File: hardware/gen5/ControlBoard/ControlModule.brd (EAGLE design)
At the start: 39 x 65.3 mm, 44 parts, among them Q1 BSS123, Q2 BSS123, U1 ATMEGA328P-AU

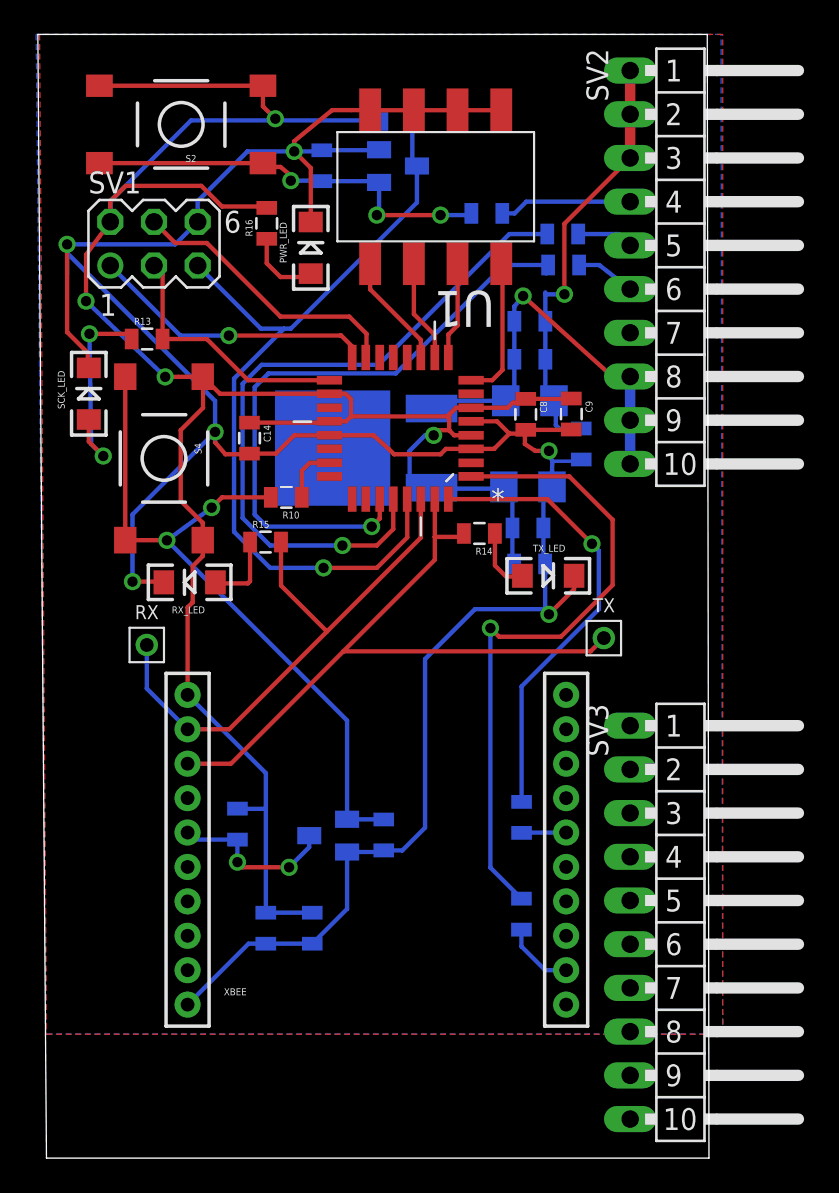
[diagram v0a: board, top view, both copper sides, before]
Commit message: connected plane to gnd and straightened out board outlines
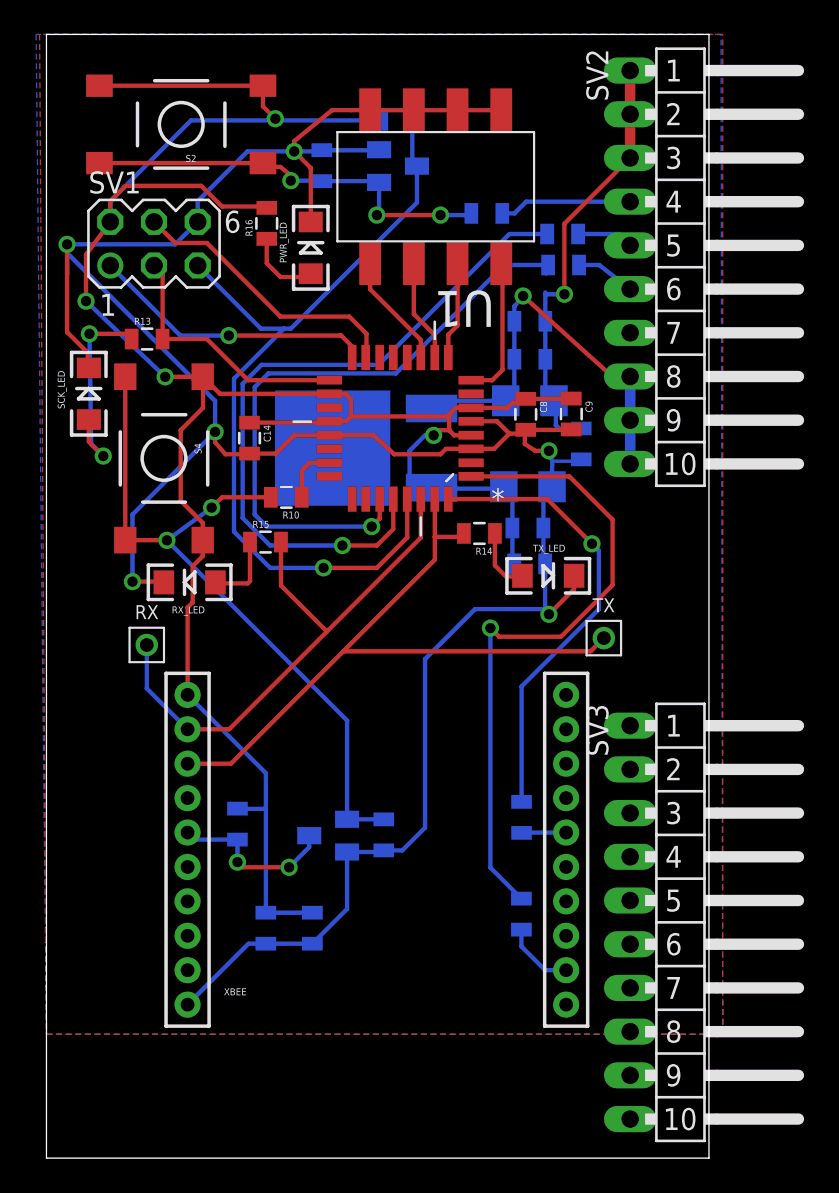
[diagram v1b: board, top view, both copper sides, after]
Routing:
- added copper zone on layer 1, net GND
- added copper zone on layer 16, net GND
- removed copper zone on layer 1, net N$4
- removed copper zone on layer 16, net N$6
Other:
- board size 39 x 65.3 mm -> 38.5 x 65.3 mm
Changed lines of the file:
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@@
 <?xml version="1.0" encoding="utf-8"?>
 <!DOCTYPE eagle SYSTEM "eagle.dtd">
-<eagle version="7.4.0">
+<eagle version="7.2.0">
 <drawing>
 <settings>
@@
 <plain>
 <wire x1="0" y1="0" x2="38.5" y2="0" width="0" layer="20"/>
-<wire x1="38.5" y1="0" x2="38.4" y2="65.3" width="0" layer="20"/>
-<wire x1="38.4" y1="65.3" x2="-0.5" y2="65.3" width="0" layer="20"/>
-<wire x1="-0.5" y1="65.3" x2="0" y2="0" width="0" layer="20"/>
+<wire x1="38.5" y1="0" x2="38.5" y2="65.3" width="0" layer="20"/>
+<wire x1="38.5" y1="65.3" x2="0" y2="65.3" width="0" layer="20"/>
+<wire x1="0" y1="65.3" x2="0" y2="0" width="0" layer="20"/>
 <dimension x1="38.5" y1="0" x2="38.4" y2="65.3" x3="51.11475" y3="32.66939375" textsize="1.778" layer="20" unit="inch"/>
 <dimension x1="39.2" y1="65.3" x2="-0.6" y2="65.3" x3="19.3" y3="70" textsize="1.778" layer="20" unit="inch"/>
@@
 <wire x1="29.4" y1="40.5" x2="30.98" y2="40.5" width="0.2032" layer="16"/>
 <wire x1="30.98" y1="40.5" x2="31.08" y2="40.6" width="0.2032" layer="16"/>
-<wire x1="16.4416" y1="42" x2="16.63" y2="41.26" width="0" layer="19" extent="1-16"/>
+<polygon width="0.254" layer="1">
+<vertex x="0" y="7.2"/>
+<vertex x="39.3" y="7.2"/>
+<vertex x="39.3" y="65.3"/>
+<vertex x="-0.4" y="65.3"/>
+</polygon>
+<polygon width="0.254" layer="16">
+<vertex x="0" y="7.2"/>
+<vertex x="39.3" y="7.2"/>
+<vertex x="39.2" y="65.3"/>
+<vertex x="-0.6" y="65.3"/>
+</polygon>
 </signal>
 <signal name="3.3V">
@@
 <wire x1="31.08" y1="42.4" x2="29.8" y2="42.4" width="0.2032" layer="16"/>
 </signal>
-<signal name="N$4">
-<polygon width="0.254" layer="1">
-<vertex x="0" y="7.2"/>
-<vertex x="39.3" y="7.2"/>
-<vertex x="39.3" y="65.3"/>
-<vertex x="-0.4" y="65.3"/>
-</polygon>
-</signal>
-<signal name="N$6">
-<polygon width="0.254" layer="16">
-<vertex x="0" y="7.2"/>
-<vertex x="39.3" y="7.2"/>
-<vertex x="39.2" y="65.3"/>
-<vertex x="-0.6" y="65.3"/>
-</polygon>
-</signal>
 </signals>

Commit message: added client code in rfc-ssl-vision-client
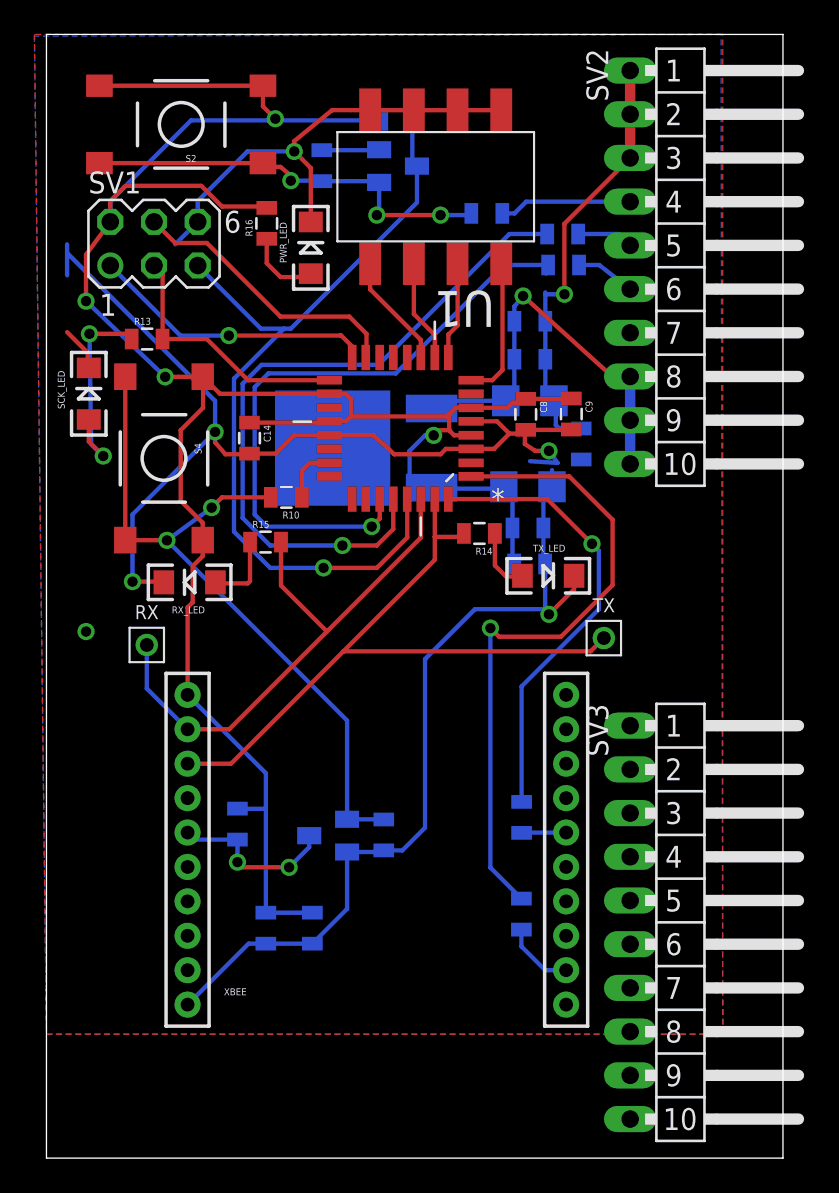
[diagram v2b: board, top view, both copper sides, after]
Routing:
- net GND: track 156.1 -> 142.8 mm
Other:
- board size 38.5 x 65.3 mm -> 42.8 x 65.3 mm
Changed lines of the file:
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@@
 <?xml version="1.0" encoding="utf-8"?>
 <!DOCTYPE eagle SYSTEM "eagle.dtd">
-<eagle version="7.2.0">
+<eagle version="7.4.0">
 <drawing>
 <settings>
@@
 <board>
 <plain>
-<wire x1="0" y1="0" x2="38.5" y2="0" width="0" layer="20"/>
-<wire x1="38.5" y1="0" x2="38.5" y2="65.3" width="0" layer="20"/>
-<wire x1="38.5" y1="65.3" x2="0" y2="65.3" width="0" layer="20"/>
+<wire x1="0" y1="0" x2="42.8" y2="0" width="0" layer="20"/>
+<wire x1="42.8" y1="0" x2="42.8" y2="65.3" width="0" layer="20"/>
+<wire x1="42.8" y1="65.3" x2="0" y2="65.3" width="0" layer="20"/>
 <wire x1="0" y1="65.3" x2="0" y2="0" width="0" layer="20"/>
 <dimension x1="38.5" y1="0" x2="38.4" y2="65.3" x3="51.11475" y3="32.66939375" textsize="1.778" layer="20" unit="inch"/>
@@
 <wire x1="19.3" y1="58.57" x2="16" y2="58.57" width="0.254" layer="16"/>
 <wire x1="16" y1="58.57" x2="15.93" y2="58.5" width="0.254" layer="16"/>
-<wire x1="15.93" y1="58.5" x2="14.4" y2="58.5" width="0.254" layer="16"/>
 <via x="14.4" y="58.5" extent="1-16" drill="0.6"/>
 <wire x1="14.4" y1="58.5" x2="14.4" y2="59.1" width="0.254" layer="1"/>
@@
 <wire x1="28.88" y1="39.01" x2="29.38" y2="39.01" width="0.254" layer="16"/>
 <wire x1="29.38" y1="39.01" x2="29.38" y2="39.98" width="0.254" layer="16"/>
-<wire x1="29.38" y1="39.98" x2="29.4" y2="40.5" width="0.254" layer="16"/>
 <wire x1="11.68" y1="58.5" x2="14.4" y2="58.5" width="0.254" layer="16"/>
-<wire x1="7.48" y1="53.1" x2="1.2" y2="53.1" width="0.254" layer="16"/>
-<via x="1.2" y="53.1" extent="1-16" drill="0.6"/>
 <wire x1="1.2" y1="51.3" x2="1.2" y2="52.6" width="0.254" layer="16"/>
 <wire x1="1.2" y1="52.6" x2="1.2" y2="53.1" width="0.254" layer="16"/>
@@
 <wire x1="22.9" y1="40.9" x2="23.2162" y2="41.2162" width="0.254" layer="1"/>
 <wire x1="23.2162" y1="41.2162" x2="24.6748" y2="41.2162" width="0.254" layer="1"/>
-<wire x1="29.4" y1="40.5" x2="29.2" y2="40.9" width="0.254" layer="16"/>
-<wire x1="29.2" y1="40.9" x2="29.2" y2="41.1" width="0.254" layer="16"/>
+<wire x1="28.1" y1="40.5" x2="29.7" y2="40.4" width="0.254" layer="16"/>
+<wire x1="29.7" y1="40.4" x2="29.2" y2="41.1" width="0.254" layer="16"/>
 <via x="29.2" y="41.1" extent="1-16" drill="0.6"/>
 <wire x1="29.2" y1="41.1" x2="28.4" y2="41.1" width="0.254" layer="1"/>
@@
 <wire x1="15.36" y1="54.4" x2="15.36" y2="57.54" width="0.254" layer="1"/>
 <wire x1="15.36" y1="57.54" x2="14.4" y2="58.5" width="0.254" layer="1"/>
-<wire x1="1.2" y1="53.1" x2="1.2" y2="48" width="0.254" layer="1"/>
 <wire x1="1.2" y1="48" x2="2.4" y2="46.8" width="0.254" layer="1"/>
 <wire x1="2.4" y1="46.8" x2="2.4" y2="45.98" width="0.254" layer="1"/>
@@
 <contactref element="U$2" pad="2"/>
 <contactref element="3.3REG" pad="DRAIN"/>
-<wire x1="29.4" y1="40.5" x2="30.98" y2="40.5" width="0.2032" layer="16"/>
-<wire x1="30.98" y1="40.5" x2="31.08" y2="40.6" width="0.2032" layer="16"/>
 <polygon width="0.254" layer="1">
 <vertex x="0" y="7.2"/>
 <vertex x="39.3" y="7.2"/>
 <vertex x="39.3" y="65.3"/>
-<vertex x="-0.4" y="65.3"/>
+<vertex x="-0.7" y="65.3"/>
 </polygon>
 <polygon width="0.254" layer="16">
@@
 <vertex x="39.3" y="7.2"/>
 <vertex x="39.2" y="65.3"/>
-<vertex x="-0.6" y="65.3"/>
+<vertex x="-0.7" y="65.2"/>
 </polygon>
+<via x="2.3" y="30.6" extent="1-16" drill="0.6"/>
 </signal>
 <signal name="3.3V">
@@
 <wire x1="30.1" y1="50.2" x2="28.99" y2="50.2" width="0.254" layer="16"/>
 <contactref element="U$2" pad="1"/>
-<wire x1="31.08" y1="42.4" x2="29.8" y2="42.4" width="0.2032" layer="16"/>
+<wire x1="31.08" y1="42.4" x2="29.8" y2="42.4" width="0.254" layer="16"/>
 </signal>
 </signals>
